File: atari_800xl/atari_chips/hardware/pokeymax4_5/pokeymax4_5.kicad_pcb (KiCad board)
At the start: 4 copper layers, 20.8 x 51.3 mm, 54 parts, among them J1 Conn_02x03_Odd_Even, J2 Conn_01x14_Pin, U2 TSV854IQ4T, U3 SN74CB3T16211DGVR, U5 SN74CB3T16211DGVR, Y1 ASE-49.152MHz

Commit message: After testing 4b first run, there are a few issues. Updated to 4b2 with: Corrected L/R output. ADC bias improvement. ADC preamp out/in- corrected. Moved silkscreen name!
git-svn-id: svn+ssh://192.168.0.3/home/svnfpga/repo/trunk@1476 d6161ac3-aae1-4d52-9b05-ea9ac36b53d3
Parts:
- removed C1: 2.2uF, Capacitor_SMD:C_0603_1608Metric
- removed R3, R4: 3k3, Resistor_SMD:R_0603_1608Metric
- added C20: 2.2uF, Capacitor_SMD:C_0603_1608Metric, F.Cu at (37.0, 21.6)
- added C21: 10uF, Capacitor_SMD:C_0603_1608Metric, F.Cu at (30.9, 24.9)
- added R24: 10k, Resistor_SMD:R_0603_1608Metric, F.Cu at (33.6, 32.0)
- added R25: 110k, Resistor_SMD:R_0603_1608Metric, F.Cu at (32.3, 24.9)
- added R26: 10k, Resistor_SMD:R_0603_1608Metric, F.Cu at (29.5, 24.9)
- added R27: 10k, Resistor_SMD:R_0603_1608Metric, F.Cu at (33.8, 24.8)
- C5, C8, C9: value C -> 18nF
- R10, R11, R7: value R -> 560
- R22, R23: value 2k7 -> DNP
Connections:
- R8 pad 2: Net-(U2-OUT) -> Net-(U2-IN4-)
- R9 pad 1: Net-(U2-OUT) -> Net-(U2-IN4-)
- U2 pad 13: /Audio output/AUD_IN_AMP -> Net-(U2-IN4-)
- U2 pad 14: Net-(U2-OUT) -> /Audio output/AUD_IN_AMP
- U4 pad C9: /Audio output/AUDL -> /Audio output/AUDR
- U4 pad D9: /Audio output/AUDR -> /Audio output/AUDL
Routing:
- net /ADC/AUD_IN: track 17.3 -> 24.8 mm
- net Net-(U2-OUT): track 5.47 -> 0.00 mm
- net Net-(U2-IN4-): track 0.00 -> 5.02 mm
- net Net-(C21-Pad2): track 0.00 -> 4.47 mm
- net GND: track 55.9 -> 59.0 mm, vias 43 -> 44
- net /Level shifter/LOUT1.B13: track 17.9 -> 15.0 mm, vias 0 -> 1
- net /Audio output/AUD_IN_AMP: track 53.5 -> 56.3 mm
- net /Level shifter/LOUT1.B15: track 17.2 -> 18.9 mm
- net Net-(U2-OUT2): track 19.6 -> 18.5 mm
- net /Audio output/AUDL: track 15.9 -> 16.8 mm
- net /ADC/AUD_IN_BIAS: track 15.1 -> 14.4 mm
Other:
- board text added: "Pokeymax 4.51"
- board text removed: "Pokeymax 4.5"

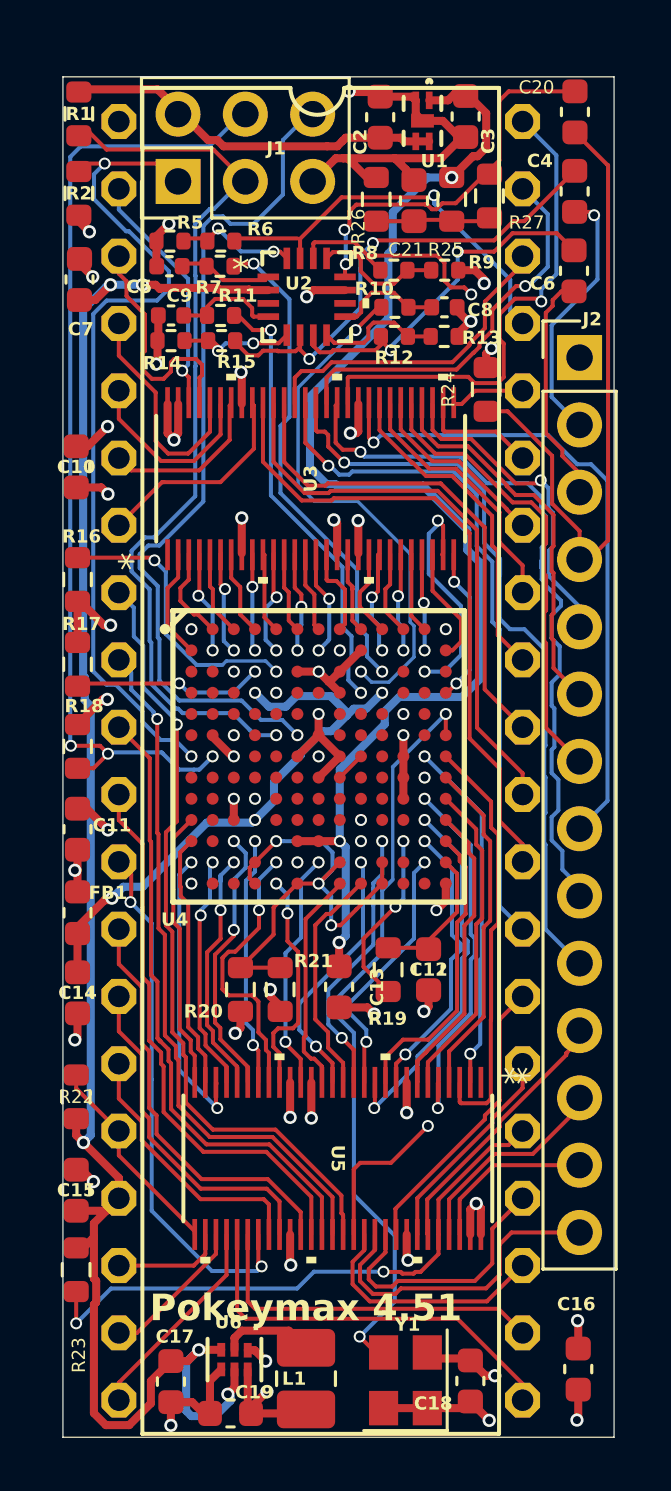
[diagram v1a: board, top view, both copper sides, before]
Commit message: Pokeymax v4_53 as produced
git-svn-id: svn+ssh://192.168.0.3/home/svnfpga/repo/trunk@1512 d6161ac3-aae1-4d52-9b05-ea9ac36b53d3
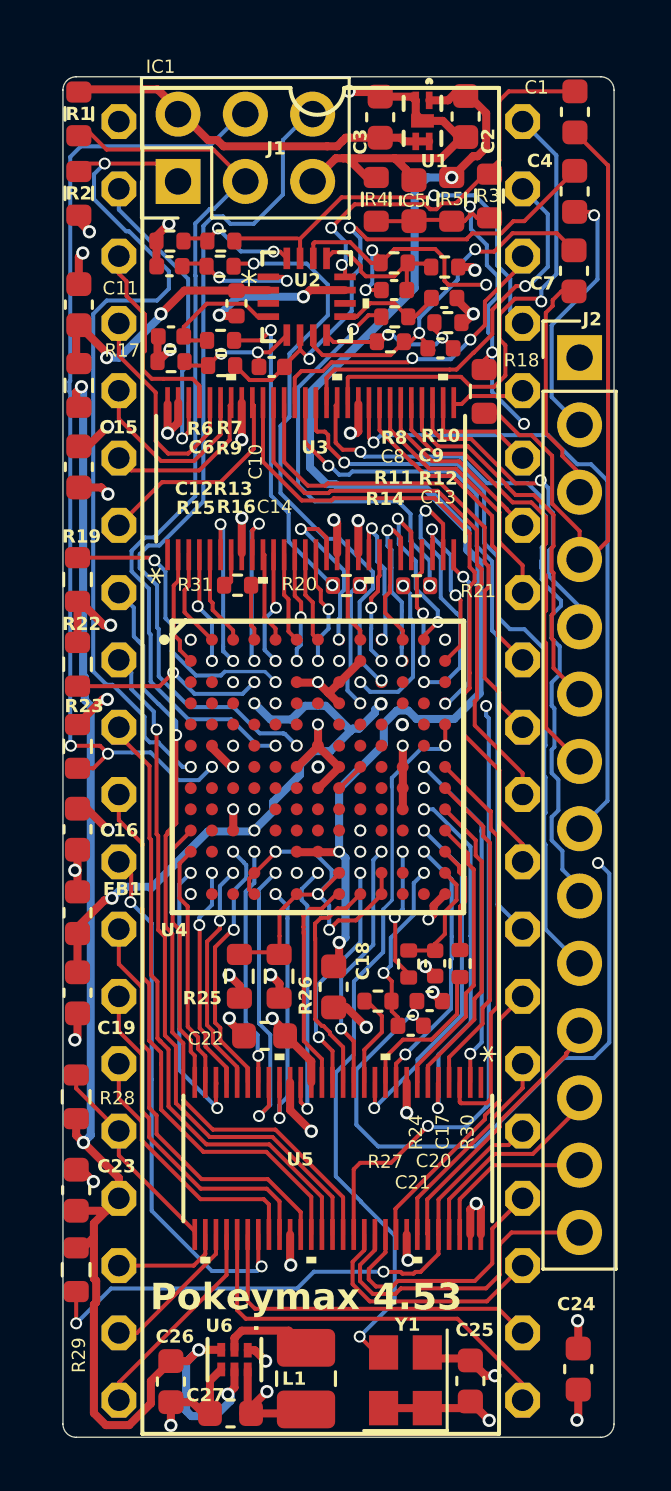
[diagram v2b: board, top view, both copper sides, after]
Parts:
- removed the C7 at (18.3, 27.9)
- removed the R24 at (33.6, 32.0)
- added C10: 0.1uF, Capacitor_SMD:C_0402_1005Metric, F.Cu at (24.2, 28.8)
- added C11: 22uF 10V, Capacitor_SMD:C_0603_1608Metric, F.Cu at (18.2, 28.9)
- added C13: 220pf C0G, Capacitor_SMD:C_0402_1005Metric, F.Cu at (31.9, 30.5)
- added C14: 220pf C0G, Capacitor_SMD:C_0402_1005Metric, F.Cu at (25.5, 31.2)
- added C20: 0.1uF, Capacitor_SMD:C_0402_1005Metric, F.Cu at (31.5, 55.1)
- added C21: 2.2nf C0G, Capacitor_SMD:C_0402_1005Metric, F.Cu at (30.8, 56.1)
- added C22: 0.1uF, Capacitor_SMD:C_0603_1608Metric, F.Cu at (25.3, 56.5)
- added C8: 220pf C0G, Capacitor_SMD:C_0402_1005Metric, F.Cu at (30.1, 28.3)
- added R17: 10, Resistor_SMD:R_0603_1608Metric, F.Cu at (18.2, 31.9)
- added R18: 220k, Resistor_SMD:R_0603_1608Metric, F.Cu at (33.5, 32.1)
- added R20: 33, Resistor_SMD:R_0402_1005Metric, F.Cu at (28.4, 39.5)
- added R21: 33, Resistor_SMD:R_0402_1005Metric, F.Cu at (31.0, 39.5)
- added R27: 1k, Resistor_SMD:R_0402_1005Metric, F.Cu at (29.5, 55.1)
- added R30: 47, Resistor_SMD:R_0402_1005Metric, F.Cu at (32.6, 53.7)
- added R31: 22, Resistor_SMD:R_0402_1005Metric, F.Cu at (24.2, 39.4)
- C1: renamed from C20; value 2.2uF -> 2.2uF C0G
- C12: renamed from C9; value 18nF -> 18nF C0G
- C17: renamed from C12; footprint Capacitor_SMD:C_0603_1608Metric -> Capacitor_SMD:C_0402_1005Metric
- C4: value 2.2uF -> 2.2uF C0G
- C6: renamed from C5; value 18nF -> 18nF C0G
- C7: renamed from C6; value 2.2uF -> 2.2uF C0G
- C9: renamed from C8; value 18nF -> 18nF C0G
- R24: renamed from R19; footprint Resistor_SMD:R_0603_1608Metric -> Resistor_SMD:R_0402_1005Metric
- R3: renamed from R27; value 10k -> 47k
- moved R13 0.94 mm to (23.6, 30.2)
- moved R16 0.94 mm to (23.6, 31.1)
- moved R24 0.80 mm to (30.7, 53.7)
- moved C12 0.79 mm to (21.7, 30.1)
- moved R15 0.79 mm to (21.7, 31.0)
- moved R12 0.54 mm to (32.2, 29.5)
- moved R25 0.50 mm to (24.3, 54.2)
- moved R26 0.50 mm to (25.8, 54.2)
- moved U4 0.40 mm to (27.3, 46.3)
- moved R11 0.36 mm to (30.2, 29.3)
- moved C9 0.35 mm to (32.0, 28.6)
- moved C17 0.35 mm to (31.7, 53.7)
- moved R8 0.28 mm to (30.1, 27.3)
- moved R14 0.25 mm to (30.0, 30.2), turned to 180 degrees
- moved C18 0.20 mm to (27.9, 54.6)
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- renumbered C10 to C15, C11 to C16, C13 to C18, C14 to C19, C3 to C2, C15 to C23, C16 to C24, C18 to C25, C17 to C26, C19 to C27, C2 to C3, C21 to C5, R9 to R10, R10 to R11, R13 to R12, R11 to R13, R12 to R14, R14 to R15, R15 to R16, R16 to R19, R17 to R22, R18 to R23, R20 to R25, R21 to R26, R22 to R28, R23 to R29, R26 to R4, R25 to R5, R5 to R6, R6 to R7, R7 to R9
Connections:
- net Net-(C21-Pad2) renamed /ADC/AUD_VBIAS
- R11 pad 1: /Audio output/AUDR -> Net-(R11-Pad1)
- R13 pad 1: /Audio output/AUDL -> Net-(R13-Pad1)
- U2 pad 2: +5V -> +5VA
- U4 pad A4: /FPGA/LIN1.A6 -> Net-(U4-T$6)
- U4 pad L13: /FPGA/LIN2.A8 -> Net-(U4-BB$19)
- U4 pad M12: /FPGA/LIN2.A10 -> /FPGA/ADC_IN
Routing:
- net /ADC/AUD_VBIAS: track 4.47 -> 58.9 mm, vias 0 -> 5
- net Net-(R11-Pad1): track 0.00 -> 15.8 mm, vias 0 -> 2
- net /Audio output/AUDR: track 20.0 -> 5.97 mm
- net Net-(R13-Pad1): track 0.00 -> 12.2 mm, vias 0 -> 2
- net /Audio output/AUDL: track 16.8 -> 4.89 mm
- net +5V: track 68.2 -> 57.3 mm, vias 5 -> 4
- net +5VA: track 0.00 -> 10.3 mm, vias 0 -> 2
- net /FPGA/ADC_IN: track 0.00 -> 6.63 mm, vias 0 -> 2
- net /FPGA/LIN2.A10: track 9.76 -> 3.70 mm, vias 2 -> 0
- net /FPGA/LIN2.A8: track 11.2 -> 5.77 mm
- net GND: track 59.0 -> 63.2 mm, vias 44 -> 46
- net Net-(U4-BB$19): track 0.00 -> 4.08 mm
- net /FPGA/LIN1.A20: track 3.07 -> 6.98 mm, vias 0 -> 2
- net /Audio output/AUD_IN_AMP: track 56.3 -> 52.4 mm, vias 2 -> 5
- net /Audio output/AUDINT: track 18.5 -> 21.9 mm
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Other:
- outline, holes or cut-outs redrawn
- board text added: "Pokeymax 4.53"
- board text removed: "Pokeymax 4.51"
